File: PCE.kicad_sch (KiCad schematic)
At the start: 0 parts

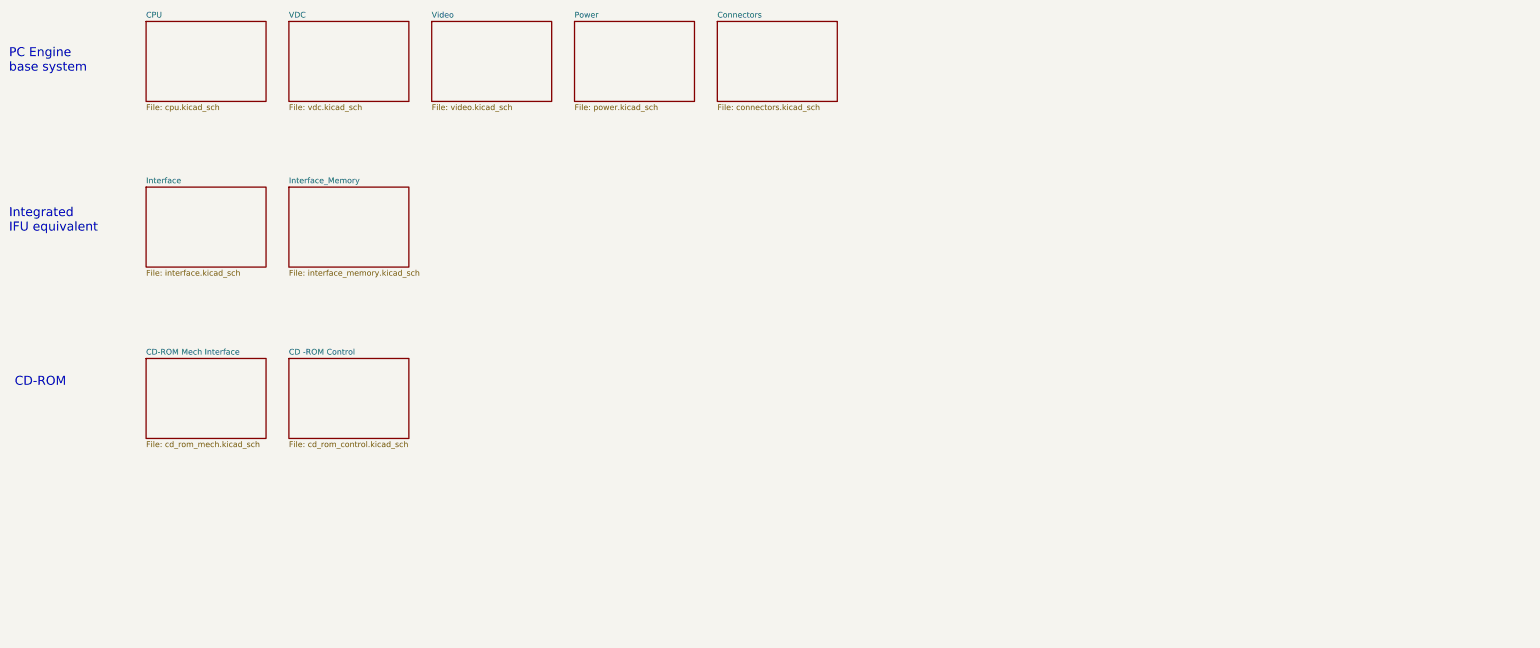
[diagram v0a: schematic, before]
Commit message: More schematic clean-up/annotation.
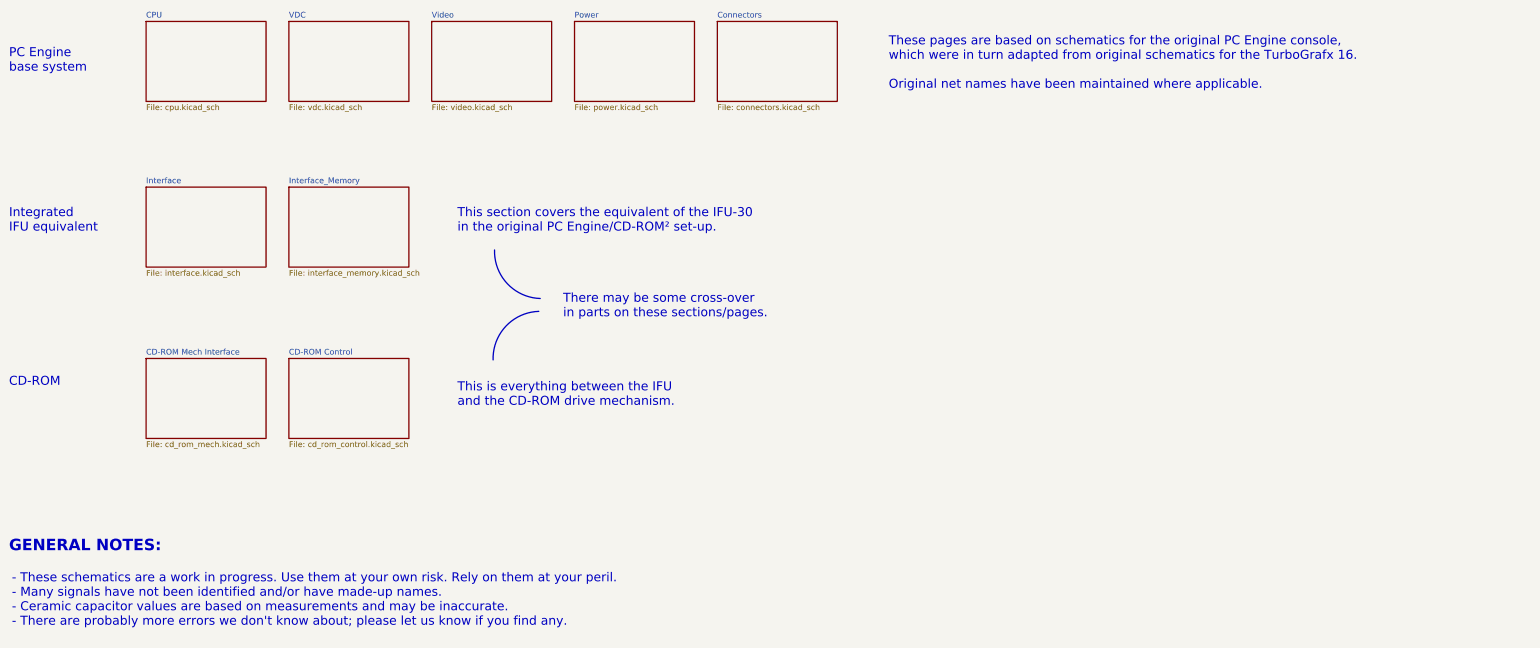
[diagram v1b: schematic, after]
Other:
- sheet CD -ROM Control renamed CD-ROM Control
- note added: "- These schematics are a work in progress. Use them at your own risk. Rely on them at your peril. - Many signals have not been identified and/or have made-up names. - Ceramic capacitor values are based on measurements and may be inaccurate. - There are probably more errors we don't know about; please let us know if you find any."
- note added: "GENERAL NOTES:"
- note added: "There may be some cross-over in parts on these sections/pages."
- note added: "These pages are based on schematics for the original PC Engine console, which were in turn adapted from original schematics for the TurboGrafx 16. Original net names have been maintained where applicable."
- note added: "This is everything between the IFU and the CD-ROM drive mechanism."
- note added: "This section covers the equivalent of the IFU-30 in the original PC Engine/CD-ROM² set-up."
- company: (none) -> By Cosam
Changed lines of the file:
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@@
   (title_block
     (title "Index")
-    (date "2023-11-01")
-    (rev "1.0")
-    (comment 1 "Reverse engineered from original PWA-3285-A board by Cosam")
-    (comment 3 "WORK IN PROGRESS")
+    (date "2023-11-03")
+    (rev "1.1")
+    (company "By Cosam")
+    (comment 1 "https://github.com/Board-Folk/PC-Engine-Duo")
+    (comment 2 "For contributions or corrections please visit:")
+    (comment 3 "Additional parts reverse engineered from original PWA-3285-A board.")
+    (comment 4 "Parts common to PC Engine adapted from TurboGrafx-16 schematics.")
   )
-  (text "CD-ROM" (at 46.99 147.32 0)
+  (arc (start 153.35 141.29) (mid 156.1932 133.7859) (end 163.51 130.495)
+    (stroke (width 0) (type default))
+    (fill (type none))
+  )
+  (arc (start 163.83 127.635) (mid 156.5143 124.3417) (end 153.67 116.84)
+    (stroke (width 0) (type default))
+    (fill (type none))
+  )
+  (text "GENERAL NOTES:" (at 45.72 184.15 0)
+    (effects (font (size 2.54 2.54) (thickness 0.254) bold) (justify left bottom))
+  )
+  (text "CD-ROM" (at 45.72 147.32 0)
     (effects (font (size 2 2)) (justify left bottom))
   )
@@
     (effects (font (size 2 2)) (justify left bottom))
   )
+  (text "This is everything between the IFU\nand the CD-ROM drive mechanism."
+    (at 145.415 151.765 0)
+    (effects (font (size 2 2)) (justify left bottom))
+  )
+  (text "- These schematics are a work in progress. Use them at your own risk. Rely on them at your peril.\n- Many signals have not been identified and/or have made-up names.\n- Ceramic capacitor values are based on measurements and may be inaccurate.\n- There are probably more errors we don't know about; please let us know if you find any."
+    (at 46.355 200.66 0)
+    (effects (font (size 2 2)) (justify left bottom))
+  )
+  (text "This section covers the equivalent of the IFU-30\nin the original PC Engine/CD-ROM² set-up."
+    (at 145.415 113.03 0)
+    (effects (font (size 2 2)) (justify left bottom))
+  )
   (text "Integrated\nIFU equivalent" (at 45.72 113.03 0)
+    (effects (font (size 2 2)) (justify left bottom))
+  )
+  (text "These pages are based on schematics for the original PC Engine console,\nwhich were in turn adapted from original schematics for the TurboGrafx 16.\n\nOriginal net names have been maintained where applicable."
+    (at 241.3 81.28 0)
+    (effects (font (size 2 2)) (justify left bottom))
+  )
+  (text "There may be some cross-over\nin parts on these sections/pages."
+    (at 168.91 132.08 0)
     (effects (font (size 2 2)) (justify left bottom))
   )
@@
     (stroke (width 0.1524) (type solid))
     (fill (color 0 0 0 0.0000))
-    (property "Sheetname" "CD -ROM Control" (at 107.95 140.2584 0)
+    (property "Sheetname" "CD-ROM Control" (at 107.95 140.2584 0)
       (effects (font (size 1.27 1.27)) (justify left bottom))
     )

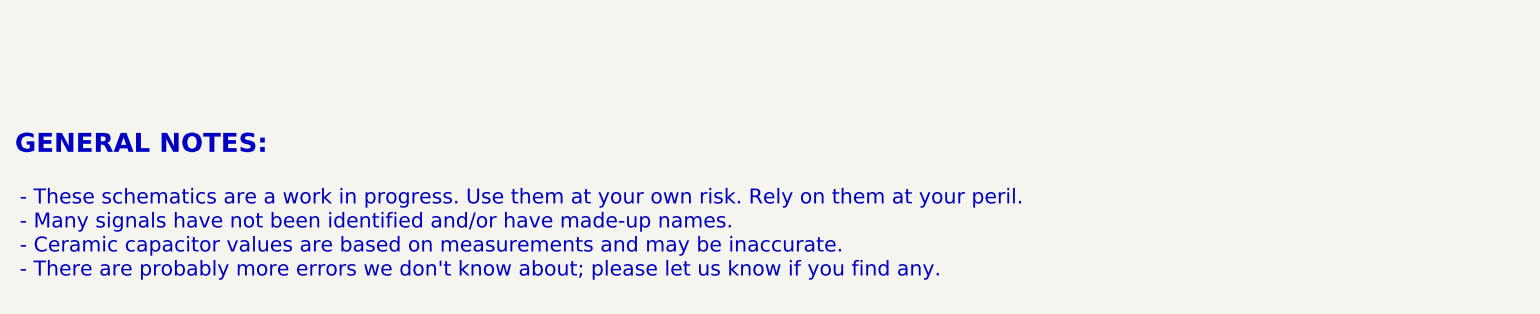
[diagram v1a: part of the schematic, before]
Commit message: Minor footprint and silkscreen changes/corrections.
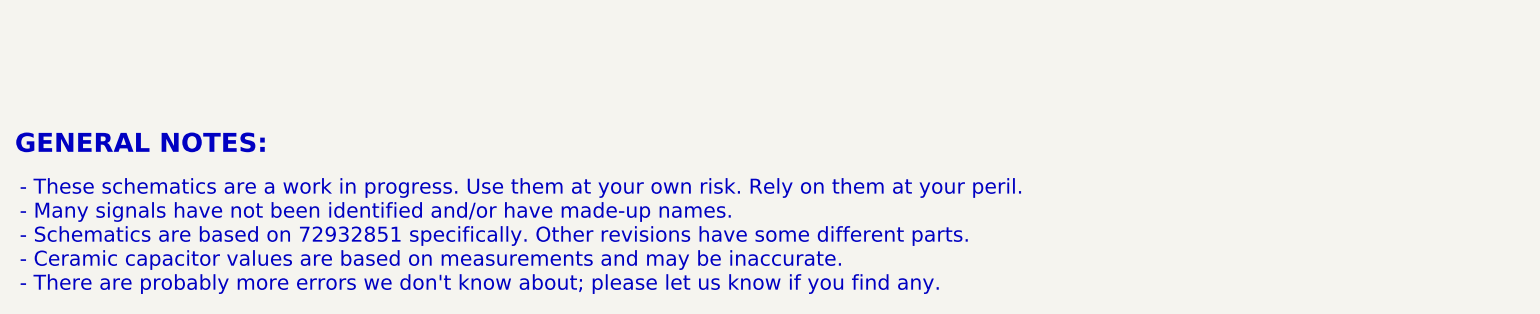
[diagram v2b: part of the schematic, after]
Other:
- note added: "- These schematics are a work in progress. Use them at your own risk. Rely on them at your peril. - Many signals have not been identified and/or have made-up names. - Schematics are based on 72932851 specifically. Other revisions have some different parts. - Ceramic capacitor values are based on measurements and may be inaccurate. - There are probably more errors we don't know about; please let u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"
- note removed: "- These schematics are a work in progress. Use them at your own risk. Rely on them at your peril. - Many signals have not been identified and/or have made-up names. - Ceramic capacitor values are based on measurements and may be inaccurate. - There are probably more errors we don't know about; please let us know if you find any."
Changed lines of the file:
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@@
     (title "Index")
     (date "2023-11-03")
-    (rev "1.1")
+    (rev "1.2")
     (company "By Cosam")
     (comment 1 "https://github.com/Board-Folk/PC-Engine-Duo")
     (comment 2 "For contributions or corrections please visit:")
-    (comment 3 "Additional parts reverse engineered from original PWA-3285-A board.")
+    (comment 3 "Additional parts reverse engineered from original PWA-3285-A 72932851 board.")
     (comment 4 "Parts common to PC Engine adapted from TurboGrafx-16 schematics.")
   )
@@
     (effects (font (size 2 2)) (justify left bottom))
   )
-  (text "- These schematics are a work in progress. Use them at your own risk. Rely on them at your peril.\n- Many signals have not been identified and/or have made-up names.\n- Ceramic capacitor values are based on measurements and may be inaccurate.\n- There are probably more errors we don't know about; please let us know if you find any."
-    (at 46.355 200.66 0)
+  (text "- These schematics are a work in progress. Use them at your own risk. Rely on them at your peril.\n- Many signals have not been identified and/or have made-up names.\n- Schematics are based on 72932851 specifically. Other revisions have some different parts.\n- Ceramic capacitor values are based on measurements and may be inaccurate.\n- There are probably more errors we don't know about; please let us know if you find any."
+    (at 46.355 202.565 0)
     (effects (font (size 2 2)) (justify left bottom))
   )
